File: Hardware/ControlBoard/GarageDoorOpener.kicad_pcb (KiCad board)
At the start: 2 copper layers, 70 x 52 mm, 48 parts, among them J1 Conn_01x04, J2 RJ45, Q1 DMG1012T-7, U1 Argon/Boron, U2 TPS56637, U3 CPC1002N, U4 VL53L1X

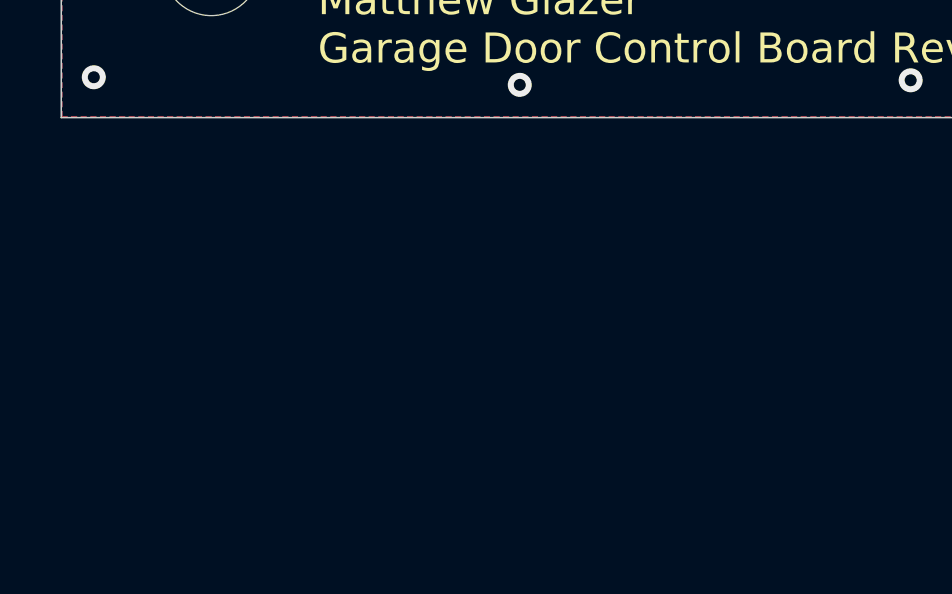
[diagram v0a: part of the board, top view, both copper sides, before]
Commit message: added some bits to the schematic, BoM updated
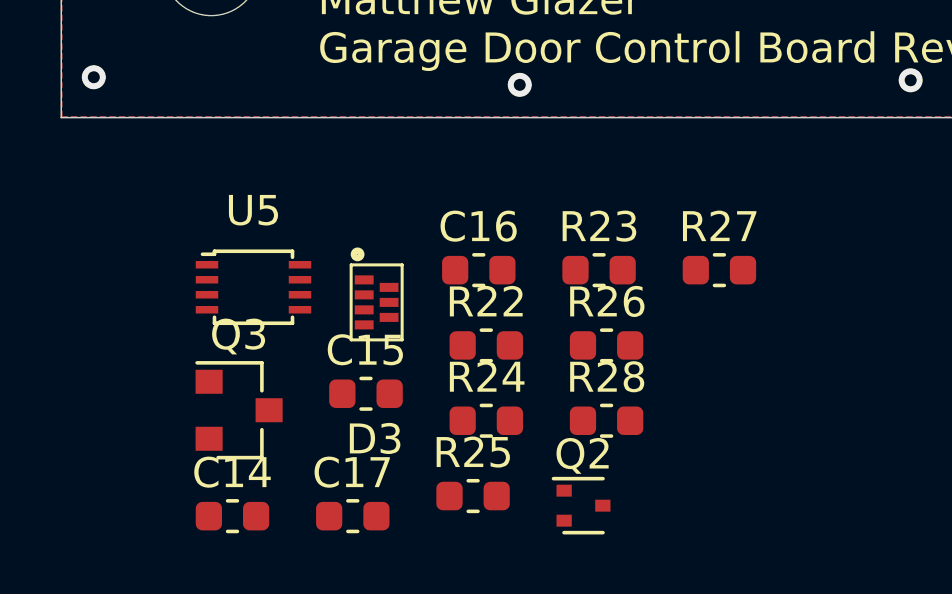
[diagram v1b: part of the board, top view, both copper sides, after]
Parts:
- added C14: 2.2uF 10V, Capacitor_SMD:C_0603_1608Metric, F.Cu at (103.7, 132.7)
- added C15: 2.2uF 10V, Capacitor_SMD:C_0603_1608Metric, F.Cu at (108.2, 128.6)
- added C16: 1uF 10V, Capacitor_SMD:C_0603_1608Metric, F.Cu at (111.9, 124.5)
- added C17: 1uF 10V, Capacitor_SMD:C_0603_1608Metric, F.Cu at (107.7, 132.7)
- added D3: PUSB3FR6Z, Global_Parts:Nexperia_XSON7, F.Cu at (108.5, 125.5)
- added Q2: DMG1012T-7, Package_TO_SOT_SMD:SOT-523, F.Cu at (115.4, 132.3)
- added Q3: SSM6J422TU,LF, Package_TO_SOT_SMD:SOT-23, F.Cu at (103.9, 129.1)
- added R22: 226, Resistor_SMD:R_0603_1608Metric, F.Cu at (112.2, 127.0)
- added R23: 226, Resistor_SMD:R_0603_1608Metric, F.Cu at (115.9, 124.5)
- added R24: 10K, Resistor_SMD:R_0603_1608Metric, F.Cu at (112.2, 129.5)
- added R25: 226, Resistor_SMD:R_0603_1608Metric, F.Cu at (111.7, 132.0)
- added R26: 10K, Resistor_SMD:R_0603_1608Metric, F.Cu at (116.2, 127.0)
- added R27: 49.9, Resistor_SMD:R_0603_1608Metric, F.Cu at (119.9, 124.5)
- added R28: 10K, Resistor_SMD:R_0603_1608Metric, F.Cu at (116.2, 129.5)
- added U5: TXB0102DCU, Package_SO:VSSOP-8_2.4x2.1mm_P0.5mm, F.Cu at (104.4, 125.0)
- R4: value 1K -> 649
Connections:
- net /SENSOR_SHUTDOWN renamed /~SENSOR_SHUTDOWN
- J1 pad 1: +5V -> Net-(J1-Pad1)
- J1 pad 2: /LED_STRIP_CLK -> Net-(J1-Pad2)
- J1 pad 3: /LED_STRIP_DATA -> Net-(J1-Pad3)
- R18 pad 2: /REED_SW2_IN -> /REED_SW2_RJ45
- R20 pad 2: /REED_SW1_IN -> /REED_SW1_RJ45
- R7 pad 2: /REED_SW1_IN -> /REED_SW1_RJ45
- R9 pad 2: /REED_SW2_IN -> /REED_SW2_RJ45
- U1 pad 22: Net-(U1-Pad22) -> /LED_PWR_TOGGLE

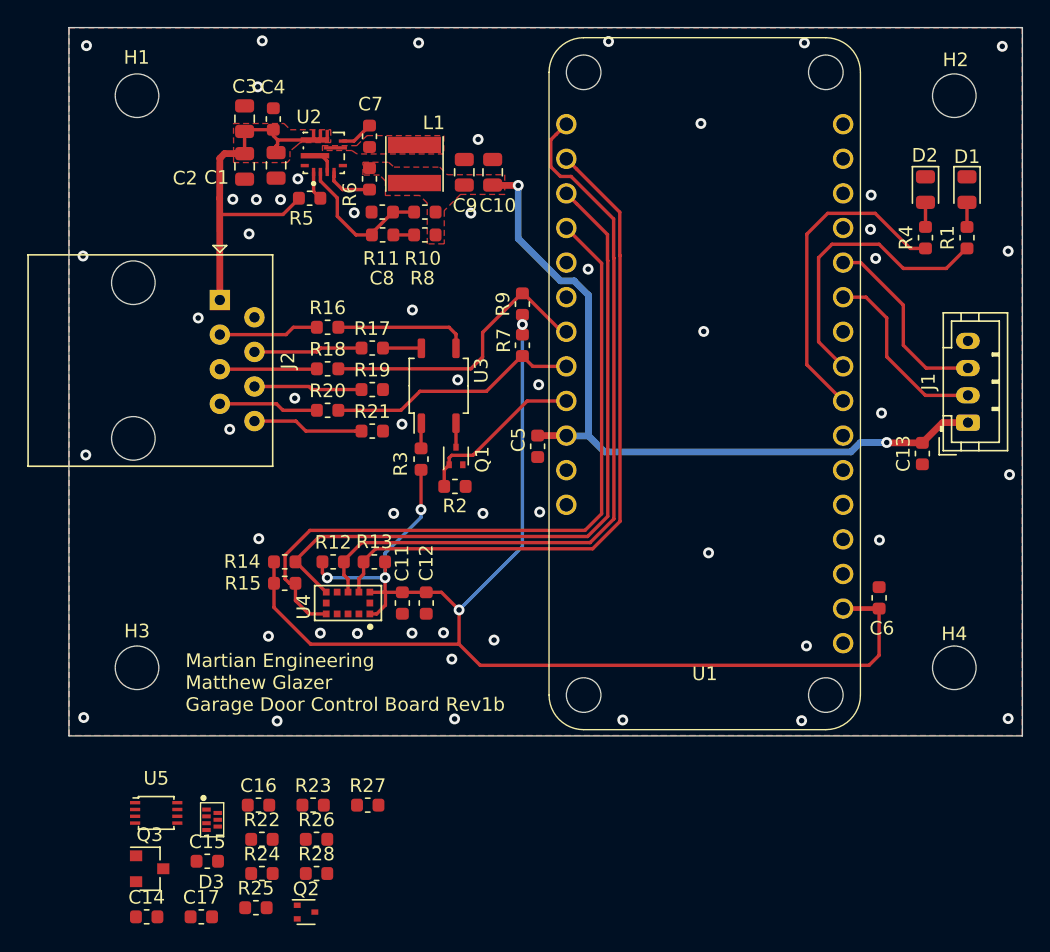
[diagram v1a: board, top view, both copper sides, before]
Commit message: finished the control board, ordered PCBs!
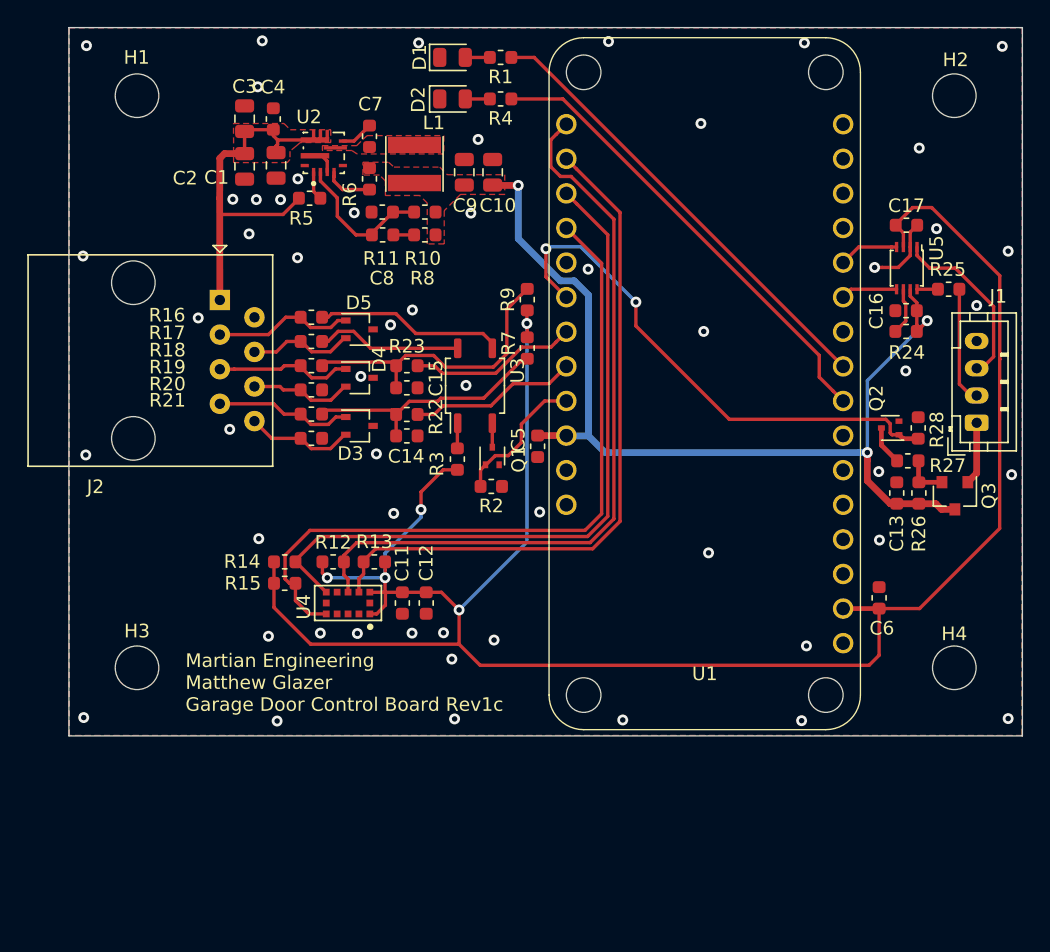
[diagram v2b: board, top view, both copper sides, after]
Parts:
- added D4: DF3A5.6LFU,LF, Package_TO_SOT_SMD:SOT-323_SC-70, F.Cu at (119.3, 93.1)
- added D5: DF3A5.6LFU,LF, Package_TO_SOT_SMD:SOT-323_SC-70, F.Cu at (119.3, 89.5)
- D3: value PUSB3FR6Z -> DF3A5.6LFU,LF; footprint Global_Parts:Nexperia_XSON7 -> Package_TO_SOT_SMD:SOT-323_SC-70
- moved C17 72.5 mm to (159.5, 81.9)
- moved R25 68.2 mm to (162.6, 86.6), turned to 180 degrees
- moved U5 68.1 mm to (159.5, 85.0), turned to 270 degrees
- moved Q3 65.1 mm to (163.0, 101.8), turned to 270 degrees
- moved R24 61.8 mm to (159.5, 89.7)
- moved C16 59.8 mm to (159.5, 88.2), turned to 180 degrees
- moved Q2 55.7 mm to (158.3, 96.8), turned to 180 degrees
- moved R28 55.0 mm to (160.4, 96.8), turned to 270 degrees
- moved R26 51.0 mm to (160.4, 101.5), turned to 90 degrees
- moved R27 47.0 mm to (159.6, 99.2)
- moved C14 40.1 mm to (122.8, 97.4)
- moved D1 39.0 mm to (126.2, 69.6), turned to 0 degrees
- moved C15 37.7 mm to (122.8, 93.8)
- moved R1 36.7 mm to (129.7, 69.6), turned to 180 degrees
- moved D2 35.4 mm to (126.2, 72.6), turned to 0 degrees
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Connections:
- D3 pad 2: GND -> Net-(D3-Pad2)
- D3 pad 3: Net-(D3-Pad3) -> GND
- J2 pad 4: Net-(D3-Pad6) -> Net-(D5-Pad2)
- J2 pad 5: Net-(D3-Pad5) -> Net-(D4-Pad1)
- J2 pad 6: Net-(D3-Pad4) -> Net-(D4-Pad2)
- J2 pad 7: Net-(D3-Pad3) -> Net-(D3-Pad1)
- J2 pad 8: Net-(D3-Pad1) -> Net-(D3-Pad2)
- R17 pad 1: Net-(D3-Pad6) -> Net-(D5-Pad2)
- R18 pad 1: Net-(D3-Pad5) -> Net-(D4-Pad1)
- R19 pad 1: Net-(D3-Pad4) -> Net-(D4-Pad2)
- R20 pad 1: Net-(D3-Pad3) -> Net-(D3-Pad1)
- R21 pad 1: Net-(D3-Pad1) -> Net-(D3-Pad2)
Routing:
- net +3V3: track 109.1 -> 153.7 mm
- net /LED_PWR_TOGGLE: track 0.00 -> 38.8 mm, vias 0 -> 2
- net /REED_SW2_RJ45: track 0.00 -> 21.9 mm
- net /REED_SW1_RJ45: track 0.00 -> 18.3 mm
- net +5V: track 56.0 -> 73.0 mm, vias 2 -> 3
- net Net-(J1-Pad3): track 0.00 -> 13.1 mm
- net /CONNECTIVITY_LED: track 21.4 -> 33.8 mm
- net /STATUS_LED: track 23.8 -> 34.5 mm
- net Net-(D4-Pad1): track 0.00 -> 10.0 mm
- net /LED_STRIP_DATA: track 14.1 -> 4.40 mm
- net /LED_STRIP_CLK: track 13.8 -> 4.17 mm
- net /REED_SW2_IN: track 21.3 -> 12.4 mm
- net Net-(J1-Pad2): track 0.00 -> 8.58 mm
- net /Relay_Ouput2: track 2.83 -> 10.8 mm
- net Net-(D3-Pad6): track 7.98 -> 0.00 mm
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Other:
- net class Default: clearance 0.2 -> 0.155
- rule trace_clearance: 0.2 -> 0.155
- rule trace_min: 0.2 -> 0.15
- board text added: "Martian Engineering Matthew Glazer Garage Door Control Board Rev1c"
- board text removed: "Martian Engineering Matthew Glazer Garage Door Control Board Rev1b"
